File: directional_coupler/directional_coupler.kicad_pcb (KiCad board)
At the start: 2 copper layers, 4 parts, among them U1 SMA_PCB_Edge_Mount, U2 SMA_PCB_Edge_Mount, U3 SMA_PCB_Edge_Mount, U4 SMA_PCB_Edge_Mount

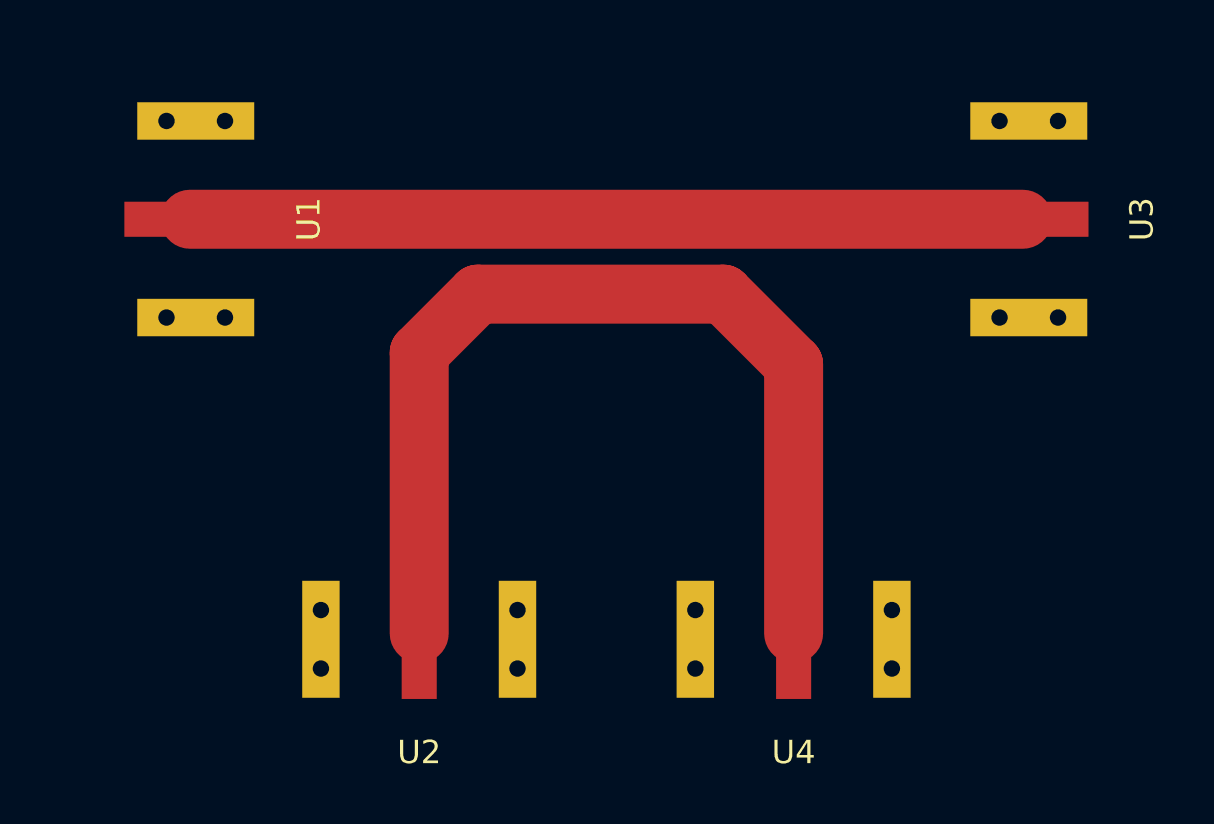
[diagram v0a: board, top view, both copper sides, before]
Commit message: Single -20 dB directional coupler
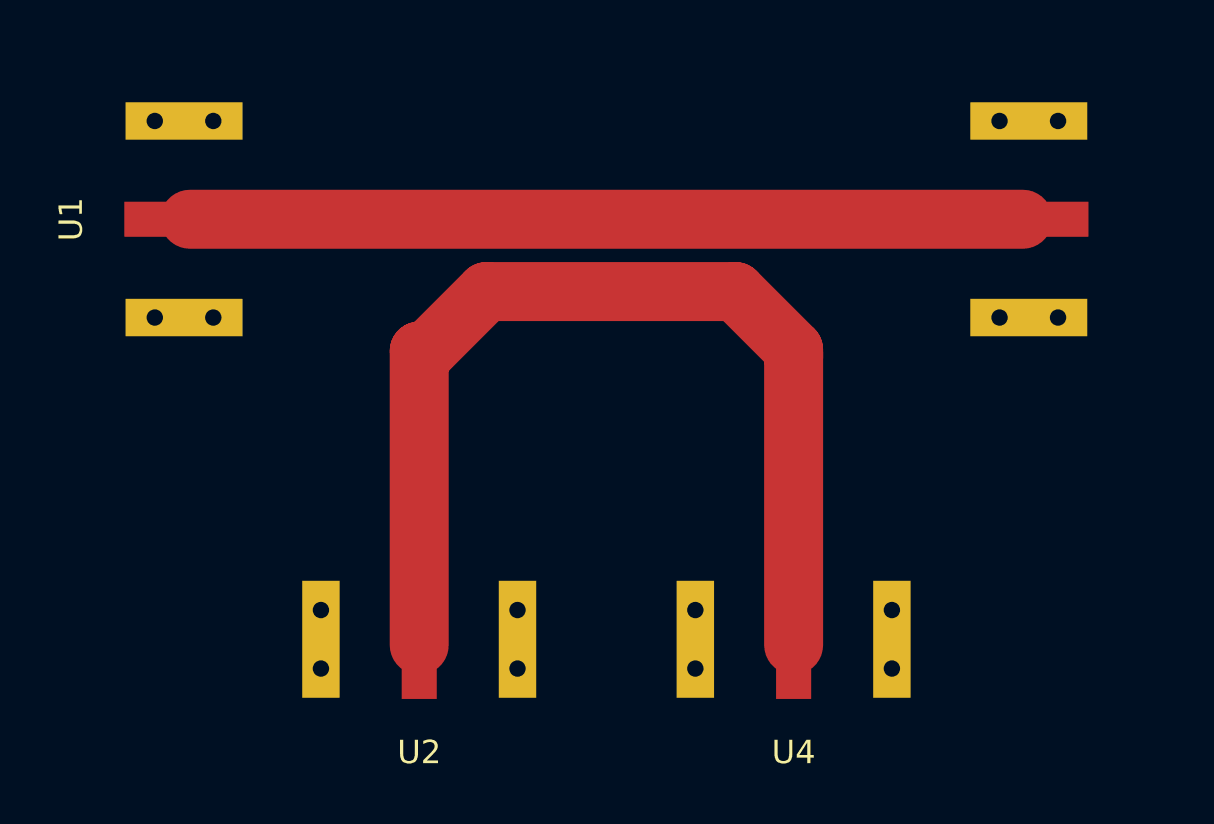
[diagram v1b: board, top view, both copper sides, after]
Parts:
- turned U1 to 270 degrees
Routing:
- net Net-(U2-Pad2): track 41.8 -> 43.5 mm
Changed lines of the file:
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@@
   (general
     (thickness 1.6)
-    (drawings 0)
-    (tracks 6)
+    (drawings 10)
+    (tracks 8)
     (zones 0)
     (modules 4)
@@
     (pad_drill 0.762)
     (pad_to_mask_clearance 0)
-    (aux_axis_origin 0 0)
+    (aux_axis_origin 82.66 104.27)
     (visible_elements FFFFFF7F)
     (pcbplotparams
@@
   )
   (module HS2_parts:SMA_EDGE_MOUNT_132255 (layer F.Cu)
-    (at 71.2 105.8 90)
+    (at 71.2 105.8 270)
     (fp_text reference U1 (at 0 5.08 90) (layer F.SilkS)
       (effects (font (size 1 1) (thickness 0.15)))
@@
       (effects (font (size 1 1) (thickness 0.15)))
     )
-    (pad 1 thru_hole rect (at -4.2 1.5 90) (size 1.6 2.5) (drill 0.7) (layers *.Cu *.Paste *.Mask)
-      (net 1 GND))
-    (pad 2 smd rect (at 0 0 90) (size 1.5 5.6) (layers F.Cu F.Paste F.Mask)
+    (pad 1 thru_hole rect (at -4.2 1.5 270) (size 1.6 2.5) (drill 0.7) (layers *.Cu *.Paste *.Mask)
+      (net 1 GND))
+    (pad 2 smd rect (at 0 0 270) (size 1.5 5.6) (layers F.Cu F.Paste F.Mask)
       (net 2 "Net-(U1-Pad2)"))
-    (pad 1 thru_hole rect (at -4.2 -1 90) (size 1.6 2.5) (drill 0.7) (layers *.Cu *.Paste *.Mask)
-      (net 1 GND))
-    (pad 3 thru_hole rect (at 4.2 1.5 90) (size 1.6 2.5) (drill 0.7) (layers *.Cu *.Paste *.Mask)
-      (net 1 GND))
-    (pad 3 thru_hole rect (at 4.2 -1 90) (size 1.6 2.5) (drill 0.7) (layers *.Cu *.Paste *.Mask)
+    (pad 1 thru_hole rect (at -4.2 -1 270) (size 1.6 2.5) (drill 0.7) (layers *.Cu *.Paste *.Mask)
+      (net 1 GND))
+    (pad 3 thru_hole rect (at 4.2 1.5 270) (size 1.6 2.5) (drill 0.7) (layers *.Cu *.Paste *.Mask)
+      (net 1 GND))
+    (pad 3 thru_hole rect (at 4.2 -1 270) (size 1.6 2.5) (drill 0.7) (layers *.Cu *.Paste *.Mask)
       (net 1 GND))
   )
@@
   (module HS2_parts:SMA_EDGE_MOUNT_132255 (layer F.Cu)
     (at 106.8 105.8 90)
-    (fp_text reference U3 (at 0 5.08 90) (layer F.SilkS)
+    (fp_text reference U3 (at 0 5.08 90) (layer F.SilkS) hide
       (effects (font (size 1 1) (thickness 0.15)))
     )
@@
       (net 1 GND))
   )
+  (gr_line (start 111.17 98.05) (end 66.94 98.05) (layer Dwgs.User) (width 0.15))
+  (gr_line (start 111.12 128.23) (end 111.17 98.05) (layer Dwgs.User) (width 0.15))
+  (gr_line (start 67 128.23) (end 111.12 128.23) (layer Dwgs.User) (width 0.15))
+  (gr_line (start 66.94 98.05) (end 67 128.23) (layer Dwgs.User) (width 0.15))
+  (dimension 13.03 (width 0.15) (layer Dwgs.User)
+    (gr_text "13.030 mm" (at 89.175 113.27) (layer Dwgs.User)
+      (effects (font (size 1 1) (thickness 0.15)))
+    )
+    (feature1 (pts (xy 95.69 104.1) (xy 95.69 112.556421)))
+    (feature2 (pts (xy 82.66 104.1) (xy 82.66 112.556421)))
+    (crossbar (pts (xy 82.66 111.97) (xy 95.69 111.97)))
+    (arrow1a (pts (xy 95.69 111.97) (xy 94.563496 112.556421)))
+    (arrow1b (pts (xy 95.69 111.97) (xy 94.563496 111.383579)))
+    (arrow2a (pts (xy 82.66 111.97) (xy 83.786504 112.556421)))
+    (arrow2b (pts (xy 82.66 111.97) (xy 83.786504 111.383579)))
+  )
+  (dimension 6.500069 (width 0.15) (layer Dwgs.User)
+    (gr_text "6.500 mm" (at 92.494122 91.268513 359.7355598) (layer Dwgs.User)
+      (effects (font (size 1 1) (thickness 0.15)))
+    )
+    (feature1 (pts (xy 95.69 103.01) (xy 95.740829 91.997085)))
+    (feature2 (pts (xy 89.19 102.98) (xy 89.240829 91.967085)))
+    (crossbar (pts (xy 89.238122 92.553499) (xy 95.738122 92.583499)))
+    (arrow1a (pts (xy 95.738122 92.583499) (xy 94.608924 93.164714)))
+    (arrow1b (pts (xy 95.738122 92.583499) (xy 94.614337 91.991885)))
+    (arrow2a (pts (xy 89.238122 92.553499) (xy 90.361907 93.145113)))
+    (arrow2b (pts (xy 89.238122 92.553499) (xy 90.36732 91.972284)))
+  )
+  (dimension 6.500069 (width 0.15) (layer Dwgs.User)
+    (gr_text "6.500 mm" (at 85.965035 91.270825 -0.3) (layer Dwgs.User)
+      (effects (font (size 1 1) (thickness 0.15)))
+    )
+    (feature1 (pts (xy 82.66 103.18) (xy 82.711741 91.969397)))
+    (feature2 (pts (xy 89.16 103.21) (xy 89.211741 91.999397)))
+    (crossbar (pts (xy 89.209035 92.585811) (xy 82.709035 92.555811)))
+    (arrow1a (pts (xy 82.709035 92.555811) (xy 83.838233 91.974596)))
+    (arrow1b (pts (xy 82.709035 92.555811) (xy 83.83282 93.147425)))
+    (arrow2a (pts (xy 89.209035 92.585811) (xy 88.08525 91.994197)))
+    (arrow2b (pts (xy 89.209035 92.585811) (xy 88.079837 93.167026)))
+  )
+  (dimension 18.790067 (width 0.15) (layer Dwgs.User)
+    (gr_text "18.790 mm" (at 79.732674 95.004848 0.1524631301) (layer Dwgs.User)
+      (effects (font (size 1 1) (thickness 0.15)))
+    )
+    (feature1 (pts (xy 89.15 103.37) (xy 89.129573 95.693424)))
+    (feature2 (pts (xy 70.36 103.42) (xy 70.339573 95.743424)))
+    (crossbar (pts (xy 70.341133 96.329843) (xy 89.131133 96.279843)))
+    (arrow1a (pts (xy 89.131133 96.279843) (xy 88.006194 96.869259)))
+    (arrow1b (pts (xy 89.131133 96.279843) (xy 88.003073 95.696422)))
+    (arrow2a (pts (xy 70.341133 96.329843) (xy 71.469193 96.913264)))
+    (arrow2b (pts (xy 70.341133 96.329843) (xy 71.466072 95.740427)))
+  )
+  (dimension 37.580048 (width 0.15) (layer Dwgs.User)
+    (gr_text "37.580 mm" (at 89.020338 98.088945 0.09147801622) (layer Dwgs.User)
+      (effects (font (size 1 1) (thickness 0.15)))
+    )
+    (feature1 (pts (xy 107.82 104.11) (xy 107.811478 98.772523)))
+    (feature2 (pts (xy 70.24 104.17) (xy 70.231478 98.832523)))
+    (crossbar (pts (xy 70.232414 99.418943) (xy 107.812414 99.358943)))
+    (arrow1a (pts (xy 107.812414 99.358943) (xy 106.686848 99.947162)))
+    (arrow1b (pts (xy 107.812414 99.358943) (xy 106.684975 98.774322)))
+    (arrow2a (pts (xy 70.232414 99.418943) (xy 71.359853 100.003564)))
+    (arrow2b (pts (xy 70.232414 99.418943) (xy 71.35798 98.830724)))
+  )
+  (dimension 0.51 (width 0.15) (layer Dwgs.User)
+    (gr_text "0.510 mm" (at 97.5 107.295 270) (layer Dwgs.User)
+      (effects (font (size 1 1) (thickness 0.15)))
+    )
+    (feature1 (pts (xy 90.41 107.55) (xy 96.786421 107.55)))
+    (feature2 (pts (xy 90.41 107.04) (xy 96.786421 107.04)))
+    (crossbar (pts (xy 96.2 107.04) (xy 96.2 107.55)))
+    (arrow1a (pts (xy 96.2 107.55) (xy 95.613579 106.423496)))
+    (arrow1b (pts (xy 96.2 107.55) (xy 96.786421 106.423496)))
+    (arrow2a (pts (xy 96.2 107.04) (xy 95.613579 108.166504)))
+    (arrow2b (pts (xy 96.2 107.04) (xy 96.786421 108.166504)))
+  )
   (segment (start 71.2 105.8) (end 106.8 105.8) (width 2.52159) (layer F.Cu) (net 2))
-  (segment (start 81 123.5) (end 81 111.5) (width 2.52159) (layer F.Cu) (net 3))
-  (segment (start 81 111.5) (end 83.5 109) (width 2.52159) (layer F.Cu) (net 3))
-  (segment (start 83.5 109) (end 94 109) (width 2.52159) (layer F.Cu) (net 3))
-  (segment (start 97 112) (end 97 123.5) (width 2.52159) (layer F.Cu) (net 3))
-  (segment (start 94 109) (end 97 112) (width 2.52159) (layer F.Cu) (net 3))
+  (segment (start 97 124) (end 97 111.5) (width 2.52159) (layer F.Cu) (net 3))
+  (segment (start 81 111.43) (end 81 124) (width 2.52159) (layer F.Cu) (net 3))
+  (segment (start 81.33 111.43) (end 81 111.43) (width 2.52159) (layer F.Cu) (net 3))
+  (segment (start 83.87 108.89) (end 81.33 111.43) (width 2.52159) (layer F.Cu) (net 3))
+  (segment (start 94.52 108.89) (end 83.87 108.89) (width 2.52159) (layer F.Cu) (net 3))
+  (segment (start 97 111.37) (end 94.52 108.89) (width 2.52159) (layer F.Cu) (net 3))
+  (segment (start 97 111.73) (end 97 111.37) (width 2.52159) (layer F.Cu) (net 3))
 )

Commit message: -20 dB coupler with ground plane
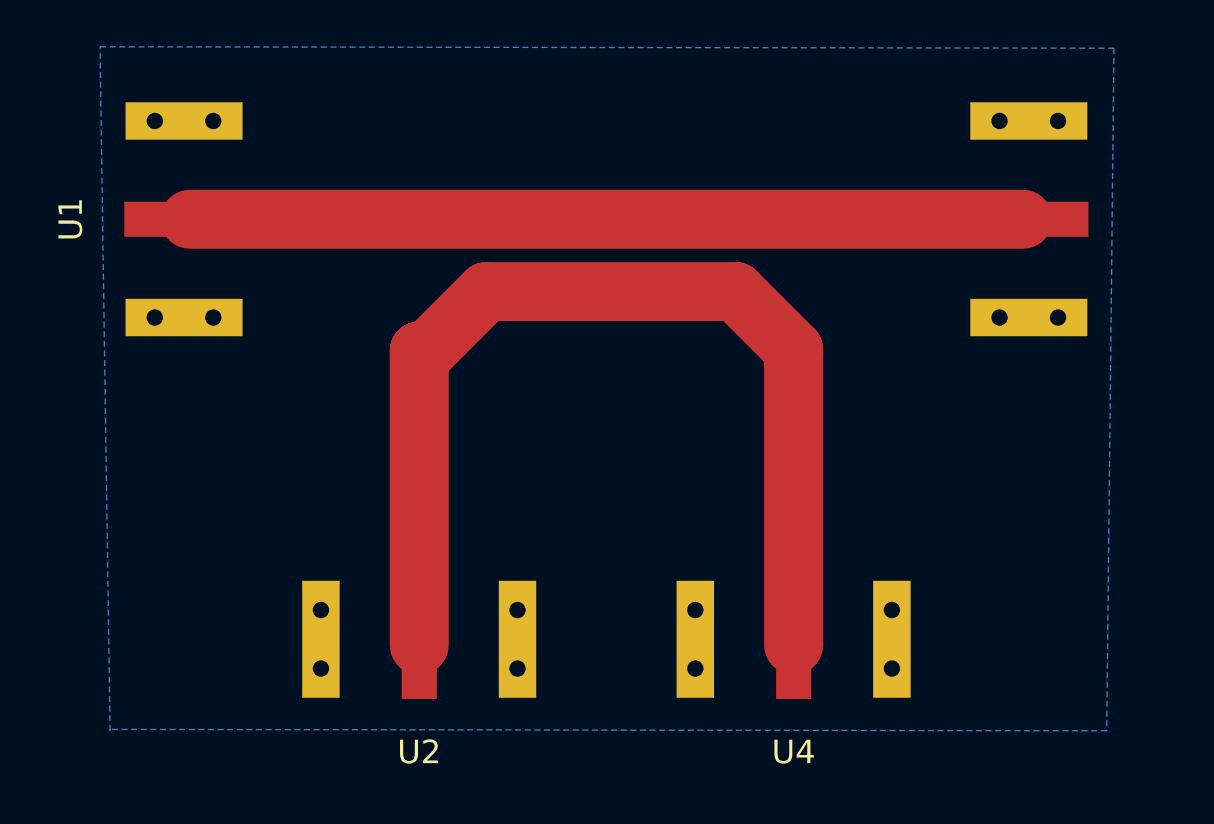
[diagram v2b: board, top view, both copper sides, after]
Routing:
- added copper zone on B.Cu, net GND
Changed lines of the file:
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@@
   (segment (start 97 111.37) (end 94.52 108.89) (width 2.52159) (layer F.Cu) (net 3))
   (segment (start 97 111.73) (end 97 111.37) (width 2.52159) (layer F.Cu) (net 3))
+  (zone (net 1) (net_name GND) (layer B.Cu) (hatch edge 0.508)
+    (connect_pads (clearance 0.508))
+    (min_thickness 0.254)
+    (fill yes (arc_segments 32) (thermal_gap 0.508) (thermal_bridge_width 0.508))
+    (polygon
+      (pts
+        (xy 110.69 98.49) (xy 110.38 127.66) (xy 67.79 127.6) (xy 67.79 127.66) (xy 67.36 98.43)
+      )
+    )
+  )
 )
